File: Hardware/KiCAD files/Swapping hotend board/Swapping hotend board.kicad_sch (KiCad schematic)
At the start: 3 parts, among them J19 PINHD_1x10_Male, J24 JST_SMD_1.0mm_Vertical

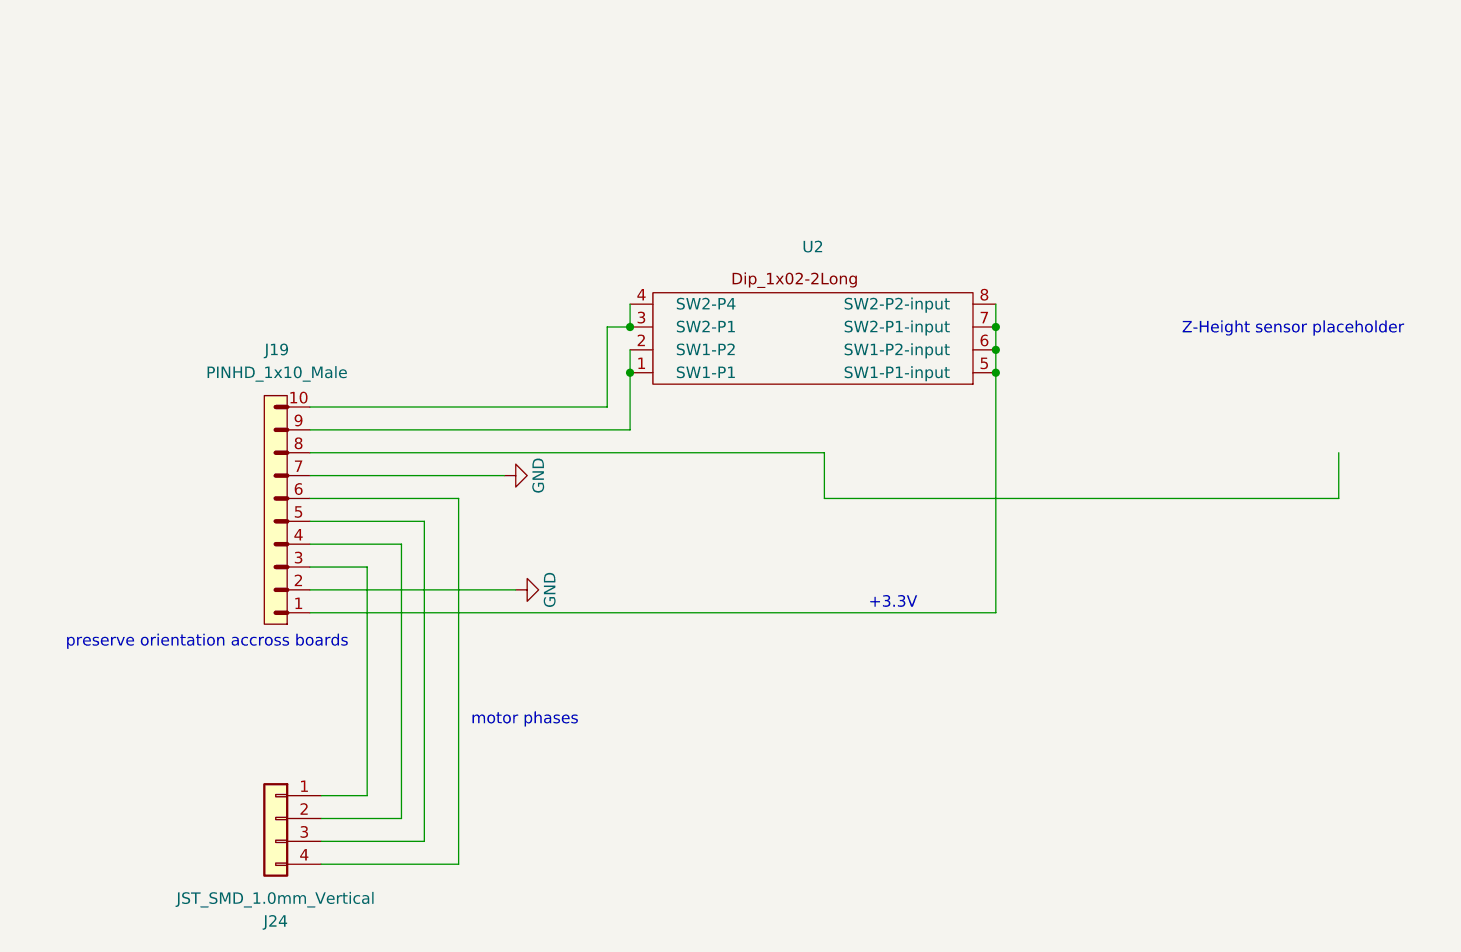
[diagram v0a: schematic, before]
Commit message: New project made to reflect layouts
New project files made in order to generate accurate layouts and create neatness.
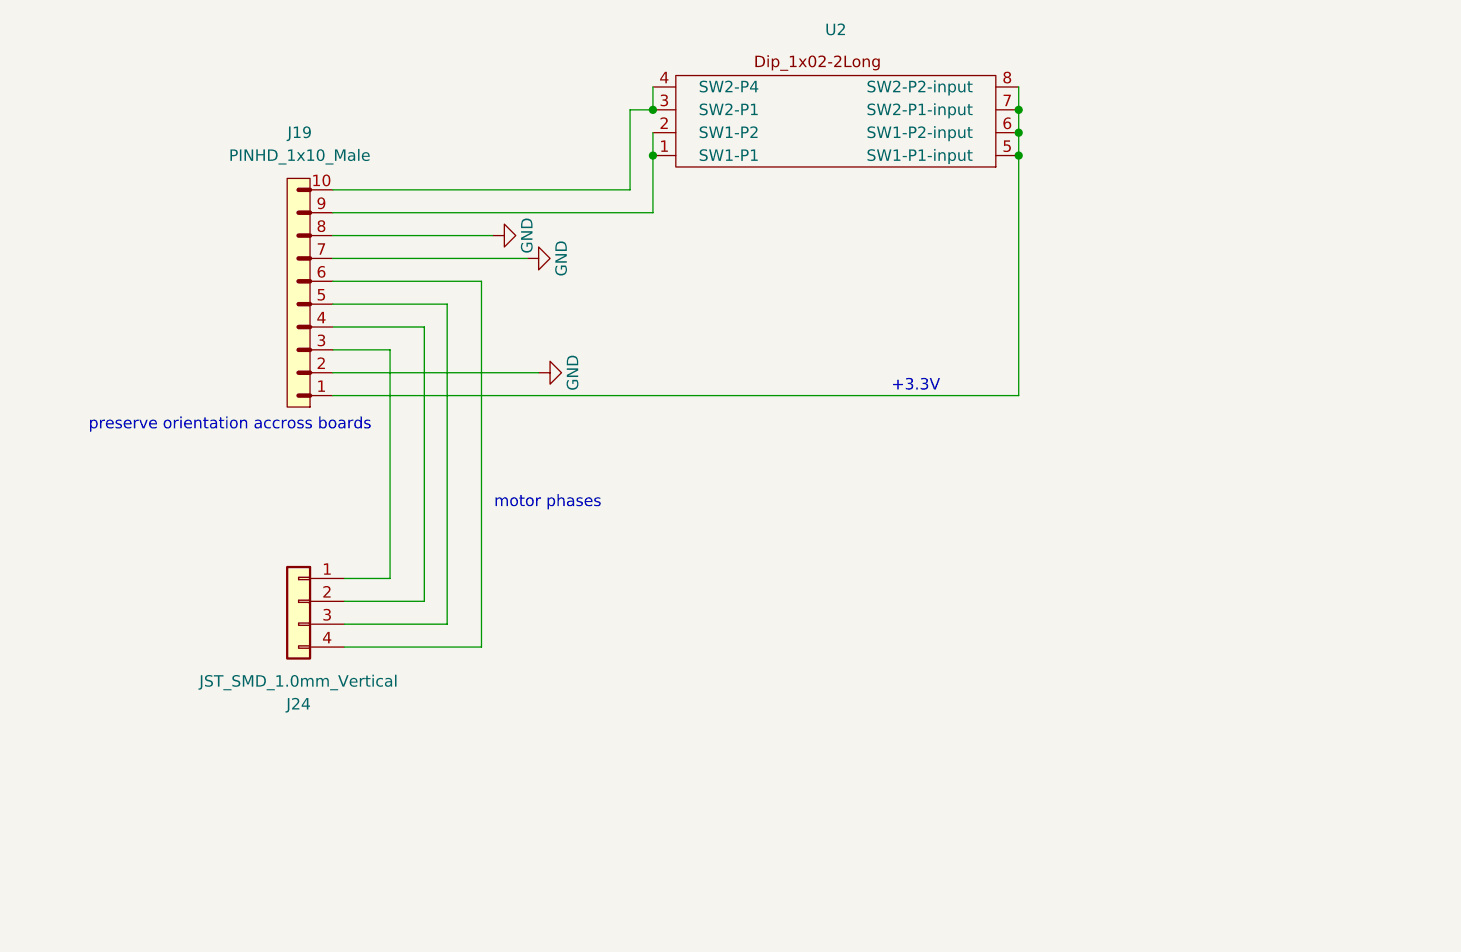
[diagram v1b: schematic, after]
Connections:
- net GND: now also J19.8
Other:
- note removed: "Z-Height sensor placeholder"

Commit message: Layout start
Was having issues with assigning pinouts on my initial schematics due to missing footprints, layouts broken into different schematics.
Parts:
- U2: footprint (none) -> Package_DIP:DIP-8_W7.62mm
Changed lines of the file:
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@@
 			)
 		)
-		(property "Footprint" ""
+		(property "Footprint" "Package_DIP:DIP-8_W7.62mm"
 			(at 92.71 29.21 0)
 			(hide yes)

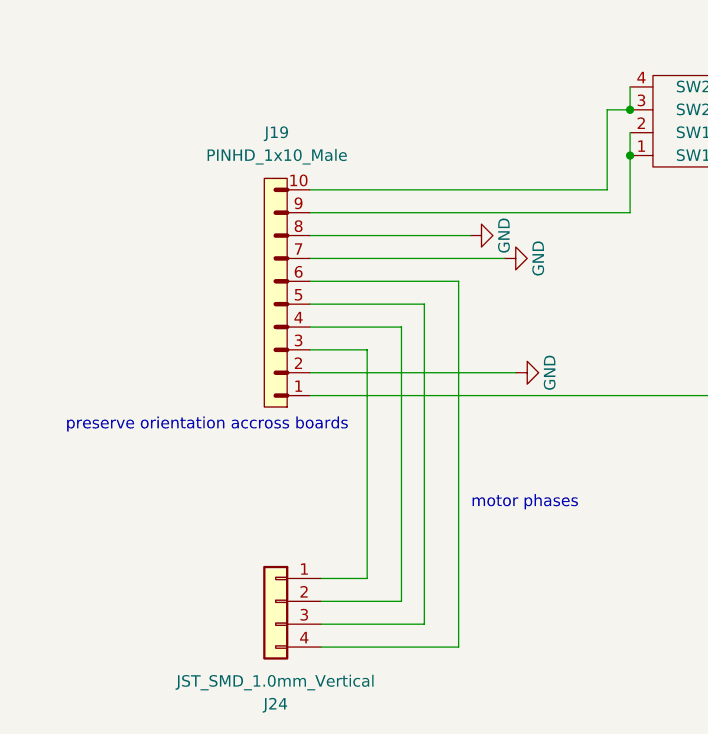
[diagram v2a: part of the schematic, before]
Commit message: general progress and adjustments
new footprint for pi reg inductor, var reg checked concurred with current part and value. re footprinted motor driver. started swapping head. adjusted some device footprints.
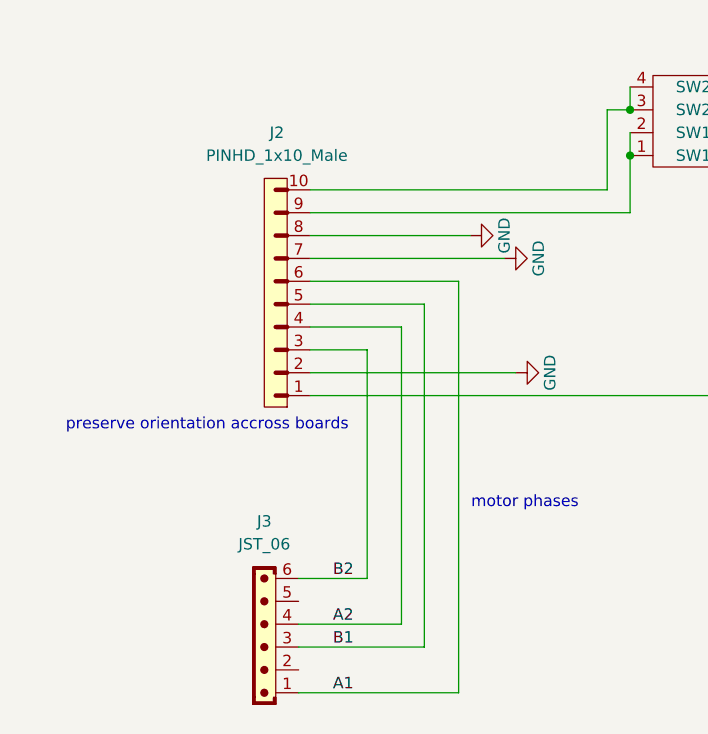
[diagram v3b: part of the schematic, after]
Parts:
- removed J19: PINHD_1x10_Male, Connector_PinHeader_2.54mm:PinHeader_1x10_P2.54mm_Vertical, symbol PCM_SL_Pin_Headers:PINHD_1x10_Male
- removed J24: JST_SMD_1.0mm_Vertical, PCM_SparkFun-Connector:JST_1x04_P1.0mm_Vertical_SMD, symbol PCM_SparkFun-Connector:Conn_01x04_JST_P1.0mm_Vertical_SMD
- added J2: PINHD_1x10_Male, Connector_PinHeader_2.54mm:PinHeader_1x10_P2.54mm_Horizontal, symbol PCM_SL_Pin_Headers:PINHD_1x10_Male
- added J3: JST_06, Connector_JST:JST_EH_S6B-EH_1x06_P2.50mm_Horizontal, symbol PCM_SL_Connectors:JST_06
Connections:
- net GND: now also J2.2, J2.7, J2.8
- net at U2.5 (SW1-P1-input), U2.6 (SW1-P2-input), U2.7 (SW2-P1-input)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: now also J2.1
- net at U2.3 (SW2-P1), U2.4 (SW2-P4): now also J2.10
- net at U2.1 (SW1-P1), U2.2 (SW1-P2): now also J2.9
- new net A1: J2.6, J3.1
- new net A2: J2.4, J3.4
- new net B1: J2.5, J3.3
- new net B2: J2.3, J3.6
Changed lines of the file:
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@@
+	(wire
+		(pts
+			(xy 60.96 92.71) (xy 43.18 92.71)
+		)
+		(stroke
+			(width 0)
+			(type default)
+		)
+	)
 	(wire
 		(pts
@@
 	(wire
 		(pts
-			(xy 54.61 82.55) (xy 45.72 82.55)
-		)
-		(stroke
-			(width 0)
-			(type default)
-		)
-	)
-	(wire
-		(pts
 			(xy 44.45 59.69) (xy 120.65 59.69)
 		)
@@
 	(wire
 		(pts
+			(xy 57.15 87.63) (xy 43.18 87.63)
+		)
+		(stroke
+			(width 0)
+			(type default)
+		)
+	)
+	(wire
+		(pts
 			(xy 44.45 44.45) (xy 66.04 44.45)
 		)
@@
 	(wire
 		(pts
-			(xy 60.96 87.63) (xy 45.72 87.63)
+			(xy 54.61 85.09) (xy 43.18 85.09)
 		)
 		(stroke
@@
 	(wire
 		(pts
-			(xy 50.8 80.01) (xy 45.72 80.01)
-		)
-		(stroke
-			(width 0)
-			(type default)
-		)
-	)
-	(wire
-		(pts
-			(xy 57.15 49.53) (xy 57.15 85.09)
-		)
-		(stroke
-			(width 0)
-			(type default)
-		)
-	)
-	(wire
-		(pts
-			(xy 54.61 52.07) (xy 54.61 82.55)
+			(xy 57.15 49.53) (xy 57.15 87.63)
+		)
+		(stroke
+			(width 0)
+			(type default)
+		)
+	)
+	(wire
+		(pts
+			(xy 54.61 52.07) (xy 54.61 85.09)
 		)
 		(stroke
@@
 	(wire
 		(pts
+			(xy 43.18 80.01) (xy 50.8 80.01)
+		)
+		(stroke
+			(width 0)
+			(type default)
+		)
+	)
+	(wire
+		(pts
 			(xy 54.61 52.07) (xy 44.45 52.07)
 		)
@@
 	(wire
 		(pts
-			(xy 45.72 85.09) (xy 57.15 85.09)
-		)
-		(stroke
-			(width 0)
-			(type default)
-		)
-	)
-	(wire
-		(pts
 			(xy 77.47 36.83) (xy 77.47 27.94)
 		)
@@
 	(wire
 		(pts
-			(xy 60.96 46.99) (xy 60.96 87.63)
-		)
-		(stroke
-			(width 0)
-			(type default)
+			(xy 60.96 46.99) (xy 60.96 92.71)
+		)
+		(stroke
+			(width 0)
+			(type default)
+		)
+	)
+	(label "A1"
+		(at 46.99 92.71 0)
+		(effects
+			(font
+				(size 1.27 1.27)
+			)
+			(justify left bottom)
+		)
+	)
+	(label "A2"
+		(at 46.99 85.09 0)
+		(effects
+			(font
+				(size 1.27 1.27)
+			)
+			(justify left bottom)
+		)
+	)
+	(label "B2"
+		(at 46.99 80.01 0)
+		(effects
+			(font
+				(size 1.27 1.27)
+			)
+			(justify left bottom)
+		)
+	)
+	(label "B1"
+		(at 46.99 87.63 0)
+		(effects
+			(font
+				(size 1.27 1.27)
+			)
+			(justify left bottom)
 		)
 	)
@@
 	)
 	(symbol
-		(lib_id "PCM_SparkFun-Connector:Conn_01x04_JST_P1.0mm_Vertical_SMD")
-		(at 40.64 82.55 0)
-		(mirror y)
-		(unit 1)
-		(body_style 1)
-		(exclude_from_sim no)
-		(in_bom yes)
-		(on_board yes)
-		(in_pos_files yes)
-		(dnp no)
-		(property "Reference" "J24"
-			(at 40.64 93.98 0)
-			(show_name no)
-			(do_not_autoplace no)
-			(effects
-				(font
-					(size 1.27 1.27)
-				)
-			)
-		)
-		(property "Value" "JST_SMD_1.0mm_Vertical"
-			(at 40.64 91.44 0)
-			(show_name no)
-			(do_not_autoplace no)
-			(effects
-				(font
-					(size 1.27 1.27)
-				)
-			)
-		)
-		(property "Footprint" "PCM_SparkFun-Connector:JST_1x04_P1.0mm_Vertical_SMD"
-			(at 40.64 92.71 0)
-			(hide yes)
-			(show_name no)
-			(do_not_autoplace no)
-			(effects
-				(font
-					(size 1.27 1.27)
-				)
-			)
-		)
-		(property "Datasheet" ""
-			(at 40.64 95.25 0)
-			(hide yes)
-			(show_name no)
-			(do_not_autoplace no)
-			(effects
-				(font
-					(size 1.27 1.27)
-				)
-			)
-		)
-		(property "Description" "4 pin JST 1mm polarized connector for I2C"
-			(at 40.64 97.79 0)
-			(hide yes)
-			(show_name no)
-			(do_not_autoplace no)
-			(effects
-				(font
-					(size 1.27 1.27)
-				)
-			)
-		)
-		(property "PROD_ID" "CONN-14483"
-			(at 40.64 100.33 0)
-			(hide yes)
-			(show_name no)
-			(do_not_autoplace no)
-			(effects
-				(font
-					(size 1.27 1.27)
-				)
-			)
-		)
-		(pin "3"
-		)
-		(pin "1"
-		)
-		(pin "4"
-		)
-		(pin "2"
-		)
-		(instances
-			(project "Swapping hotend board"
-				(path "/d55638fc-8c18-4352-a8d7-1cc5ced4de31"
-					(reference "J24")
-					(unit 1)
-				)
-			)
-		)
-	)
-	(symbol
 		(lib_id "PCM_SparkFun-PowerSymbol:GND")
 		(at 67.31 57.15 90)
@@
 		(dnp no)
 		(fields_autoplaced yes)
-		(property "Reference" "J19"
+		(property "Reference" "J2"
 			(at 40.765 30.48 0)
 			(show_name no)
@@
 			)
 		)
-		(property "Footprint" "Connector_PinHeader_2.54mm:PinHeader_1x10_P2.54mm_Vertical"
+		(property "Footprint" "Connector_PinHeader_2.54mm:PinHeader_1x10_P2.54mm_Horizontal"
 			(at 41.91 67.31 0)
 			(hide yes)
@@
 			)
 		)
+		(pin "4"
+		)
+		(pin "5"
+		)
+		(pin "9"
+		)
+		(pin "6"
+		)
+		(pin "7"
+		)
+		(pin "10"
+		)
+		(pin "1"
+		)
+		(pin "8"
+		)
+		(pin "2"
+		)
 		(pin "3"
-		)
-		(pin "2"
-		)
-		(pin "5"
-		)
-		(pin "1"
-		)
-		(pin "7"
-		)
-		(pin "8"
-		)
-		(pin "4"
-		)
-		(pin "9"
-		)
-		(pin "6"
-		)
-		(pin "10"
 		)
 		(instances
 			(project "Swapping hotend board"
 				(path "/d55638fc-8c18-4352-a8d7-1cc5ced4de31"
-					(reference "J19")
+					(reference "J2")
 					(unit 1)
 				)
+			)
+		)
+	)
+	(symbol
+		(lib_id "PCM_SL_Connectors:JST_06")
+		(at 39.37 86.36 180)
+		(unit 1)
+		(body_style 1)
+		(exclude_from_sim no)
+		(in_bom yes)
+		(on_board yes)
+		(in_pos_files yes)
+		(dnp no)
+		(fields_autoplaced yes)
+		(property "Reference" "J3"
+			(at 39.37 73.66 0)
+			(show_name no)
+			(do_not_autoplace no)
+			(effects
+				(font
+					(size 1.27 1.27)
+				)
+			)
+		)
+		(property "Value" "JST_06"
+			(at 39.37 76.2 0)
+			(show_name no)
+			(do_not_autoplace no)
+			(effects
+				(font
+					(size 1.27 1.27)
+				)
+			)
+		)
+		(property "Footprint" "Connector_JST:JST_EH_S6B-EH_1x06_P2.50mm_Horizontal"
+			(at 39.37 97.79 0)
+			(hide yes)
+			(show_name no)
+			(do_not_autoplace no)
+			(effects
+				(font
+					(size 1.27 1.27)
+				)
+			)
+		)
+		(property "Datasheet" ""
+			(at 39.37 97.79 0)
+			(hide yes)
+			(show_name no)
+			(do_not_autoplace no)
+			(effects
+				(font
+					(size 1.27 1.27)
+				)
+			)
+		)
+		(property "Description" "JST Connector  6 pins"
+			(at 39.37 86.36 0)
+			(hide yes)
+			(show_name no)
+			(do_not_autoplace no)
+			(effects
+				(font
+					(size 1.27 1.27)
+				)
+			)
+		)
+		(pin "1"
+		)
+		(pin "5"
+		)
+		(pin "2"
+		)
+		(pin "6"
+		)
+		(pin "4"
+		)
+		(pin "3"
+		)
+		(instances
+			(project "Swapping hotend board"
+				(path "/d55638fc-8c18-4352-a8d7-1cc5ced4de31"
+					(reference "J3")
+					(unit 1)
+				)

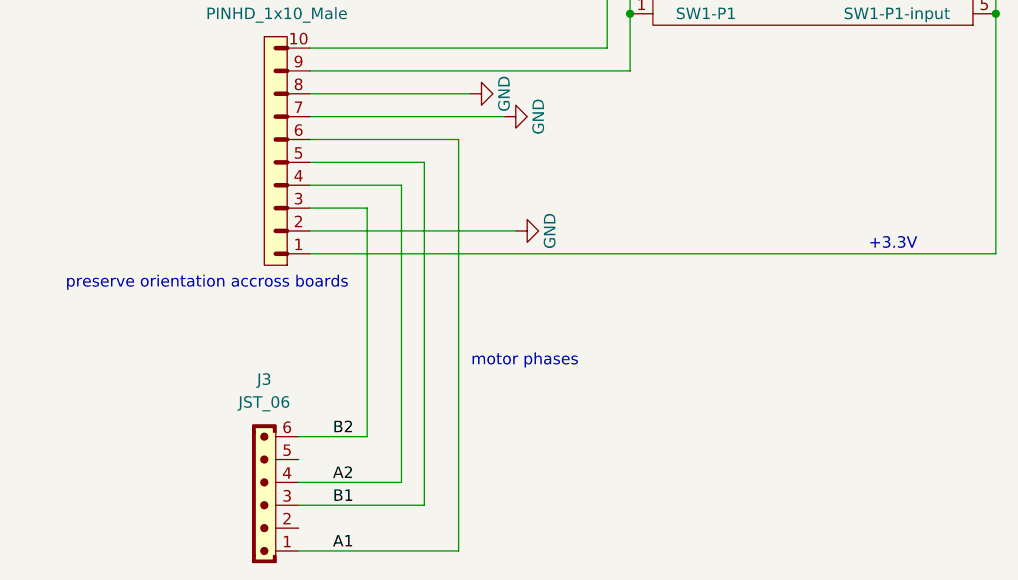
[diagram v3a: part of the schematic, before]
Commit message: DRV 8825 and regulator purchased set
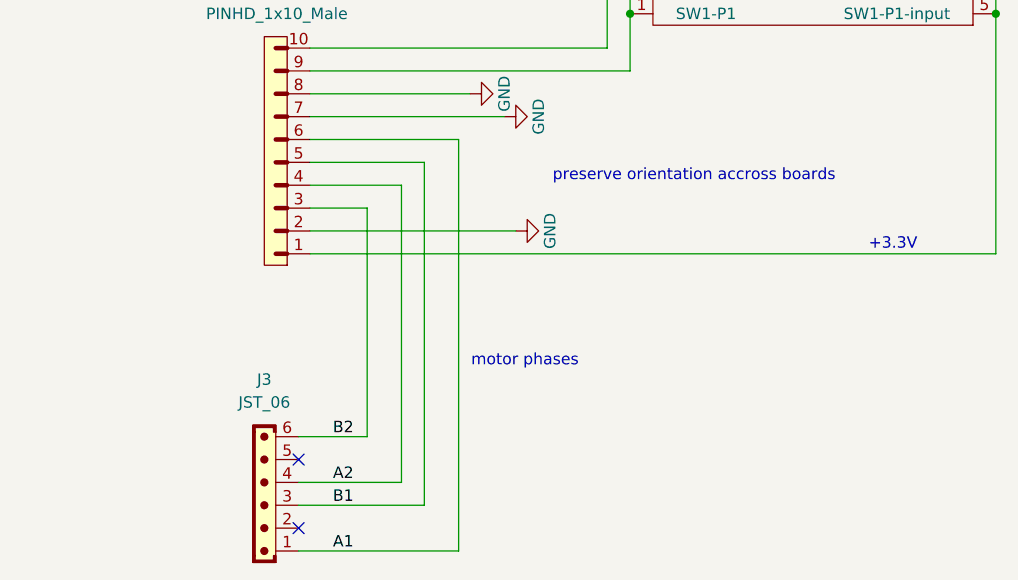
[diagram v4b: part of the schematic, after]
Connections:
- no-connect marks 0 -> 2
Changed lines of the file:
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@@
 	(text "preserve orientation accross boards\n"
 		(exclude_from_sim no)
-		(at 33.02 62.992 0)
+		(at 87.122 51.054 0)
 		(effects
 			(font
@@
 		(color 0 0 0 0)
 	)
+	(no_connect
+		(at 43.18 90.17)
+	)
+	(no_connect
+		(at 43.18 82.55)
+	)
 	(wire

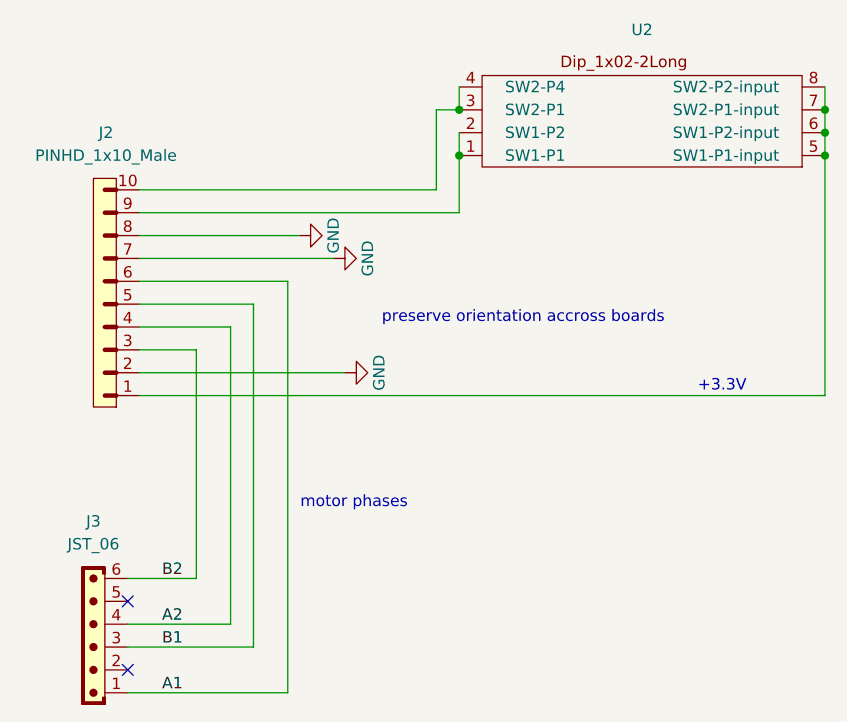
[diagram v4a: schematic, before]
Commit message: Compatability mods
basic modifications to work toward compatability between boards physically on the hotend
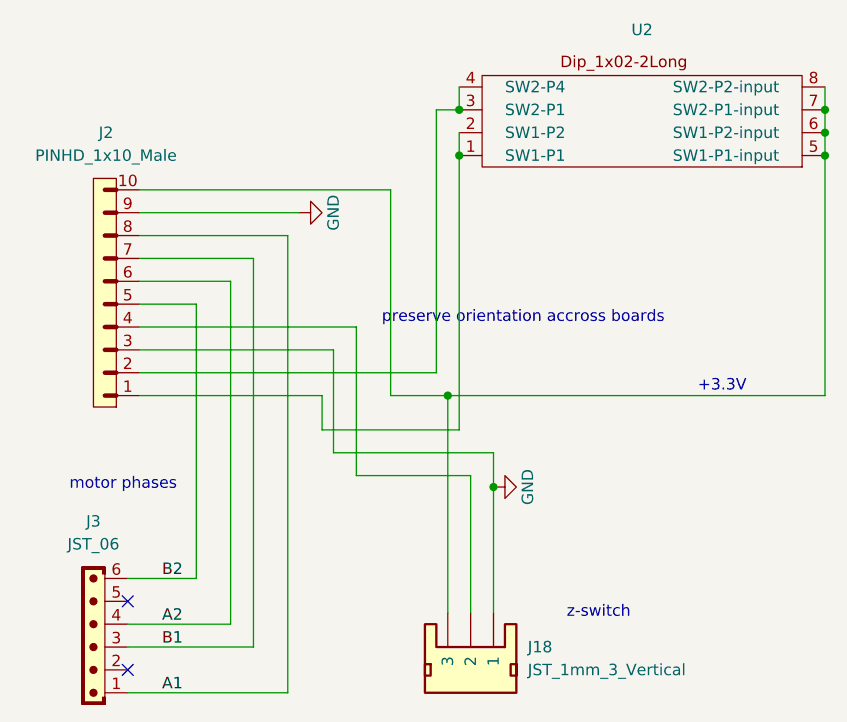
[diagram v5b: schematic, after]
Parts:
- added J18: JST_1mm_3_Vertical, PCM_SparkFun-Connector:JST_1x03_P1.0mm_Vertical_SMD, symbol PCM_SparkFun-Connector:Conn_01x03_JST_P1.0mm_Vertical_SMD
- J2: footprint Connector_PinHeader_2.54mm:PinHeader_1x10_P2.54mm_Horizontal -> Connector_PinHeader_2.54mm:PinHeader_1x10_P2.54mm_Vertical
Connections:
- net A1: now also J2.8; no longer J2.6
- net A2: now also J2.6; no longer J2.4
- net B1: now also J2.7; no longer J2.5
- net B2: now also J2.5; no longer J2.3
- net GND: now also J2.3, J2.9, J18.1; no longer J2.2, J2.7, J2.8
- net at U2.5 (SW1-P1-input), U2.6 (SW1-P2-input), U2.7 (SW2-P1-input)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: now also J2.10, J18.3; no longer J2.1
- net at U2.3 (SW2-P1), U2.4 (SW2-P4): now also J2.2; no longer J2.10
- net at U2.1 (SW1-P1), U2.2 (SW1-P2): now also J2.1; no longer J2.9
- new net: J18.2, J2.4
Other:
- note added: "z-switch"

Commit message: V1 boards after final board invoice
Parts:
- J18: footprint PCM_SparkFun-Connector:JST_1x03_P1.0mm_Vertical_SMD -> PCM_SparkFun-Connector:1x03_P2.54mm
- J3: footprint Connector_JST:JST_EH_S6B-EH_1x06_P2.50mm_Horizontal -> PCM_4ms_Connector:Pins_1x06_2.54mm_TH_SWD
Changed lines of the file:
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@@
 			)
 		)
-		(property "Footprint" "Connector_JST:JST_EH_S6B-EH_1x06_P2.50mm_Horizontal"
+		(property "Footprint" "PCM_4ms_Connector:Pins_1x06_2.54mm_TH_SWD"
 			(at 39.37 97.79 0)
 			(hide yes)
@@
 			)
 		)
-		(property "Footprint" "PCM_SparkFun-Connector:JST_1x03_P1.0mm_Vertical_SMD"
+		(property "Footprint" "PCM_SparkFun-Connector:1x03_P2.54mm"
 			(at 72.39 88.9 0)
 			(hide yes)
